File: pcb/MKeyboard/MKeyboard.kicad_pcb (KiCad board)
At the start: 6 copper layers, 57.1 x 114.3 mm, 90 parts, among them J1 USB_C_Receptacle_USB2.0, SW0 SW_Push, SW1 SW_Push, SW10 SW_Push, SW11 SW_Push, SW12 SW_Push, SW2 SW_Push, SW20 SW_Push, SW21 SW_Push, SW22 SW_Push, SW3 SW_DIP_x01, SW30 SW_Push, SW31 SW_Push, SW32 SW_Push, SW40 SW_Push, SW41 SW_Push, SW42 SW_Push, U1 AT90USB646-AU, Y1 Crystal_GND24

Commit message: placement
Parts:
- moved R33 41.6 mm to (106.6, 116.1), turned to 270 degrees
- moved R32 40.6 mm to (103.0, 116.1), turned to 270 degrees
- moved R31 40.0 mm to (99.6, 116.5), turned to 270 degrees
- moved C2 39.5 mm to (96.8, 96.0)
- moved C9 39.5 mm to (96.8, 108.7)
- moved R61 39.5 mm to (95.5, 115.1)
- moved C1 39.5 mm to (110.7, 92.2)
- moved C3 39.5 mm to (96.8, 102.4)
- moved C8 39.5 mm to (104.4, 92.2)
- moved R52 39.4 mm to (112.5, 151.0)
- moved R53 39.4 mm to (115.1, 151.0)
- moved R54 39.4 mm to (117.6, 151.0)
- moved U1 39.2 mm to (107.7, 103.5)
- moved R8 38.7 mm to (98.4, 149.1)
- moved R7 38.7 mm to (98.4, 151.6)
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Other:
- board size 57.1 x 114.3 mm -> 57.1 x 88.8 mm

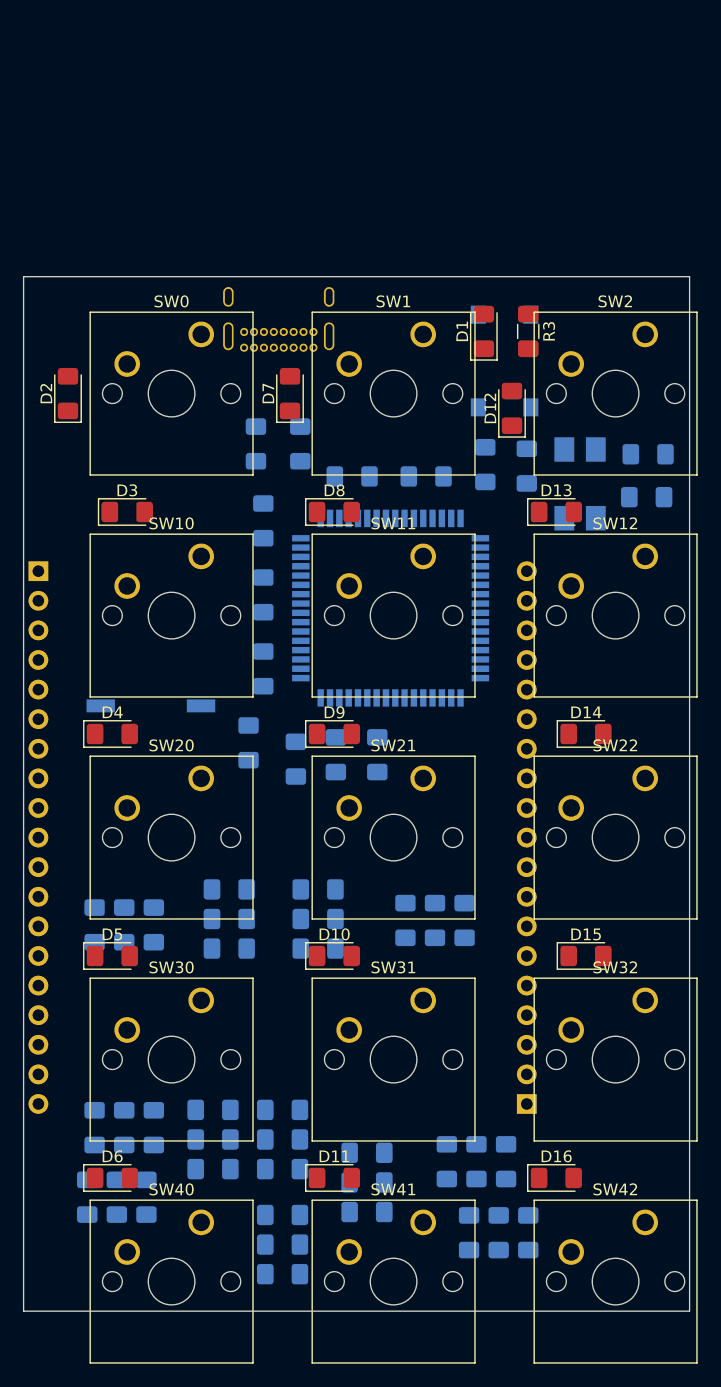
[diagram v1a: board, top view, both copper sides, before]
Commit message: smaller components, positioning
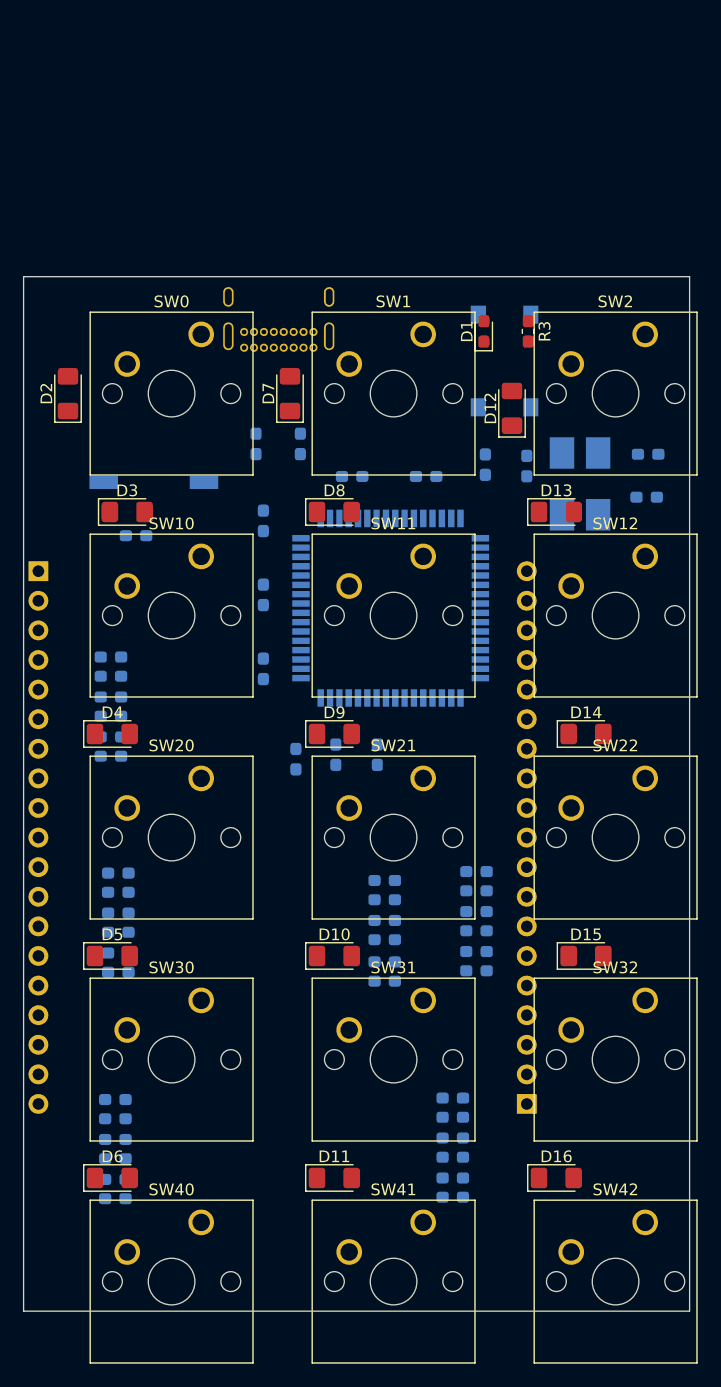
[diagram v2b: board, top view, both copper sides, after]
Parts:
- C1, C2, C3, C4, C5, C7, C8, C9: footprint Capacitor_SMD:C_1206_3216Metric_Pad1.42x1.75mm_HandSolder -> Capacitor_SMD:C_0603_1608Metric_Pad1.05x0.95mm_HandSolder
- D1: footprint LED_SMD:LED_1206_3216Metric_Pad1.42x1.75mm_HandSolder -> LED_SMD:LED_0603_1608Metric_Pad1.05x0.95mm_HandSolder
- R1, R10, R11, R12, R13, R14, R15, R16, R17, R18, R19, R2, R20, R21, R22, R23, R24, R25, R26, R27, R3, R31, R32, R33, R34, R35, R36, R4, R43, R44, R45, R5, R52, R53, R54, R58, R59, R6, R60, R61, R62, R7, R8, R9: footprint Resistor_SMD:R_1206_3216Metric_Pad1.42x1.75mm_HandSolder -> Resistor_SMD:R_0603_1608Metric_Pad1.05x0.95mm_HandSolder
- Y1: footprint Crystal:Crystal_SMD_7050-4Pin_7.0x5.0mm -> Crystal:Crystal_SMD_0603-4Pin_6.0x3.5mm_HandSoldering
- moved R54 26.3 mm to (107.2, 126.9), turned to 0 degrees
- moved R27 23.0 mm to (83.7, 107.7), turned to 0 degrees
- moved R53 22.1 mm to (107.2, 130.3), turned to 0 degrees
- moved R21 21.9 mm to (84.3, 126.2), turned to 0 degrees
- moved R24 20.9 mm to (83.7, 109.3)
- moved R15 20.4 mm to (84.3, 127.9)
- moved R61 20.2 mm to (85.9, 97.3), turned to 180 degrees
- moved R23 20.1 mm to (83.7, 112.8)
- moved R9 20.1 mm to (107.2, 128.5)
- moved R26 19.6 mm to (83.7, 111.1), turned to 0 degrees
- moved R14 19.5 mm to (84.3, 131.3)
- moved R22 19.4 mm to (83.7, 116.2)
- moved R8 19.3 mm to (107.2, 132.0)
- moved SW3 19.2 mm to (87.4, 92.7)
- moved R13 18.7 mm to (84.3, 134.7)
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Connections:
- J1 pad A5: Net-(J1-PadA5) -> (no net)
- J1 pad A8: Net-(J1-PadA8) -> (no net)
- J1 pad B5: Net-(J1-PadB5) -> (no net)
- J1 pad B8: Net-(J1-PadB8) -> (no net)
- U1 pad 1: Net-(U1-Pad1) -> (no net)
- U1 pad 10: Net-(U1-Pad10) -> (no net)
- U1 pad 11: Net-(U1-Pad11) -> (no net)
- U1 pad 12: Net-(U1-Pad12) -> (no net)
- U1 pad 13: Net-(U1-Pad13) -> (no net)
- U1 pad 14: Net-(U1-Pad14) -> (no net)
- U1 pad 15: Net-(U1-Pad15) -> (no net)
- U1 pad 16: Net-(U1-Pad16) -> (no net)
- U1 pad 17: Net-(U1-Pad17) -> (no net)
- U1 pad 18: Net-(U1-Pad18) -> (no net)
- U1 pad 19: Net-(U1-Pad19) -> (no net)
- U1 pad 2: Net-(U1-Pad2) -> (no net)
- U1 pad 54: Net-(U1-Pad54) -> (no net)
- U1 pad 55: Net-(U1-Pad55) -> (no net)
- U1 pad 56: Net-(U1-Pad56) -> (no net)
- U1 pad 57: Net-(U1-Pad57) -> (no net)
- U1 pad 58: Net-(U1-Pad58) -> (no net)
- U1 pad 59: Net-(U1-Pad59) -> (no net)
- U1 pad 60: Net-(U1-Pad60) -> (no net)
- U1 pad 61: Net-(U1-Pad61) -> (no net)
- U1 pad 62: Net-(U1-Pad62) -> (no net)
- U1 pad 9: Net-(U1-Pad9) -> (no net)

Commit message: Most 0-ohm resisters are routed.
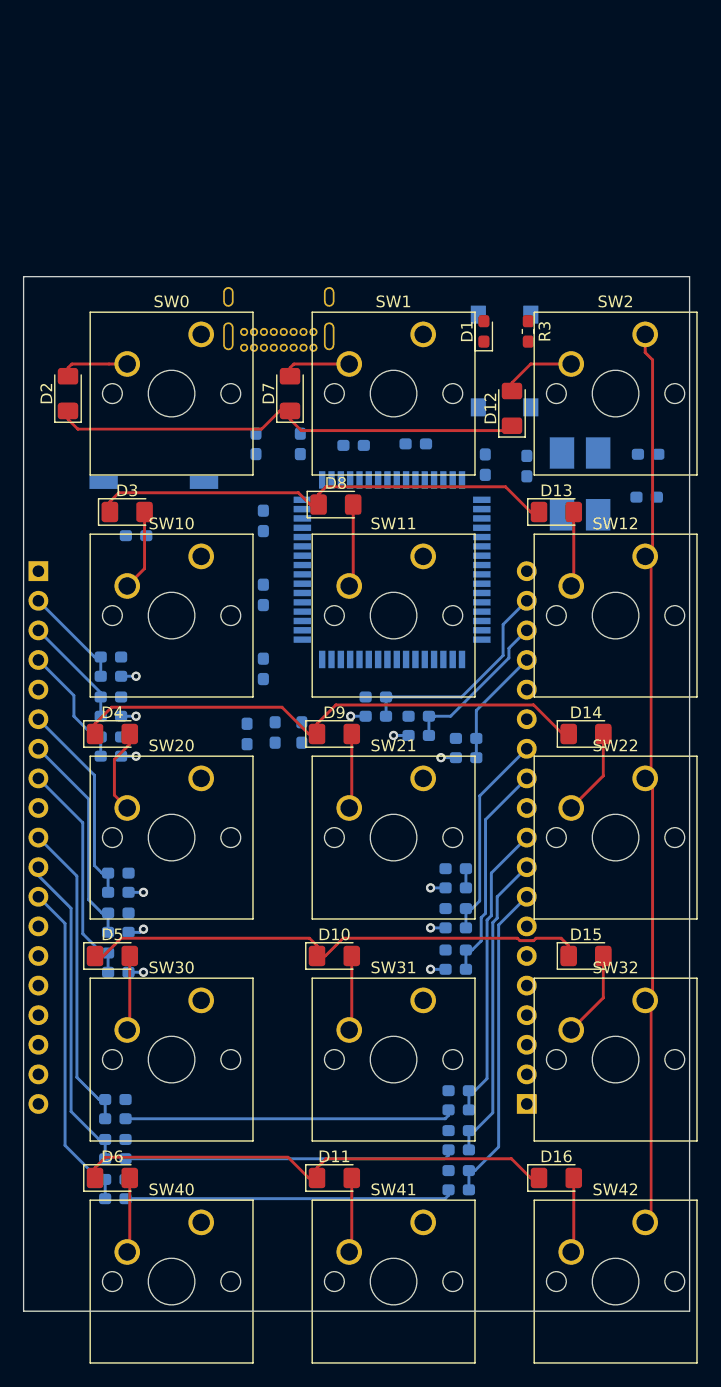
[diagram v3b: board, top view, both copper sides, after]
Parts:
- moved R16 18.3 mm to (114.2, 116.3)
- moved R58 18.3 mm to (114.2, 114.7)
- moved R17 17.5 mm to (110.1, 114.4)
- moved R59 17.5 mm to (110.1, 112.8)
- moved R18 17.3 mm to (106.4, 112.8)
- moved R60 17.3 mm to (106.4, 111.1)
- moved R33 6.75 mm to (100.1, 114.2)
- moved R54 6.18 mm to (113.3, 125.9)
- moved R9 6.18 mm to (113.3, 127.5)
- moved R52 6.18 mm to (113.3, 132.8)
- moved R53 6.18 mm to (113.3, 129.3)
- moved R7 6.18 mm to (113.3, 134.5)
- moved R8 6.18 mm to (113.3, 130.9)
- moved R32 5.54 mm to (97.8, 114.2)
- moved R31 4.71 mm to (95.4, 114.3)
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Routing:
- net /col2: track 0.00 -> 106.4 mm
- net /col1: track 0.00 -> 105.9 mm
- net /col0: track 0.00 -> 105.5 mm
- net /con_l0_0: track 0.00 -> 67.0 mm, vias 0 -> 1
- net /con_l0_1: track 0.00 -> 65.8 mm, vias 0 -> 1
- net /con_l0_2: track 0.00 -> 64.5 mm, vias 0 -> 1
- net /con_r0_0: track 0.00 -> 64.4 mm, vias 0 -> 1
- net /con_r0_1: track 0.00 -> 63.1 mm, vias 0 -> 1
- net /con_r0_2: track 0.00 -> 61.9 mm, vias 0 -> 1
- net /con_r1_0: track 0.00 -> 58.1 mm, vias 0 -> 1
- net /con_l1_0: track 0.00 -> 56.0 mm, vias 0 -> 1
- net /con_r1_1: track 0.00 -> 55.1 mm, vias 0 -> 1
- net /con_l1_1: track 0.00 -> 52.4 mm, vias 0 -> 1
- net /con_l1_2: track 0.00 -> 49.1 mm, vias 0 -> 1
- net /row2: track 0.00 -> 45.6 mm
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
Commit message: Most of the non-power routing.
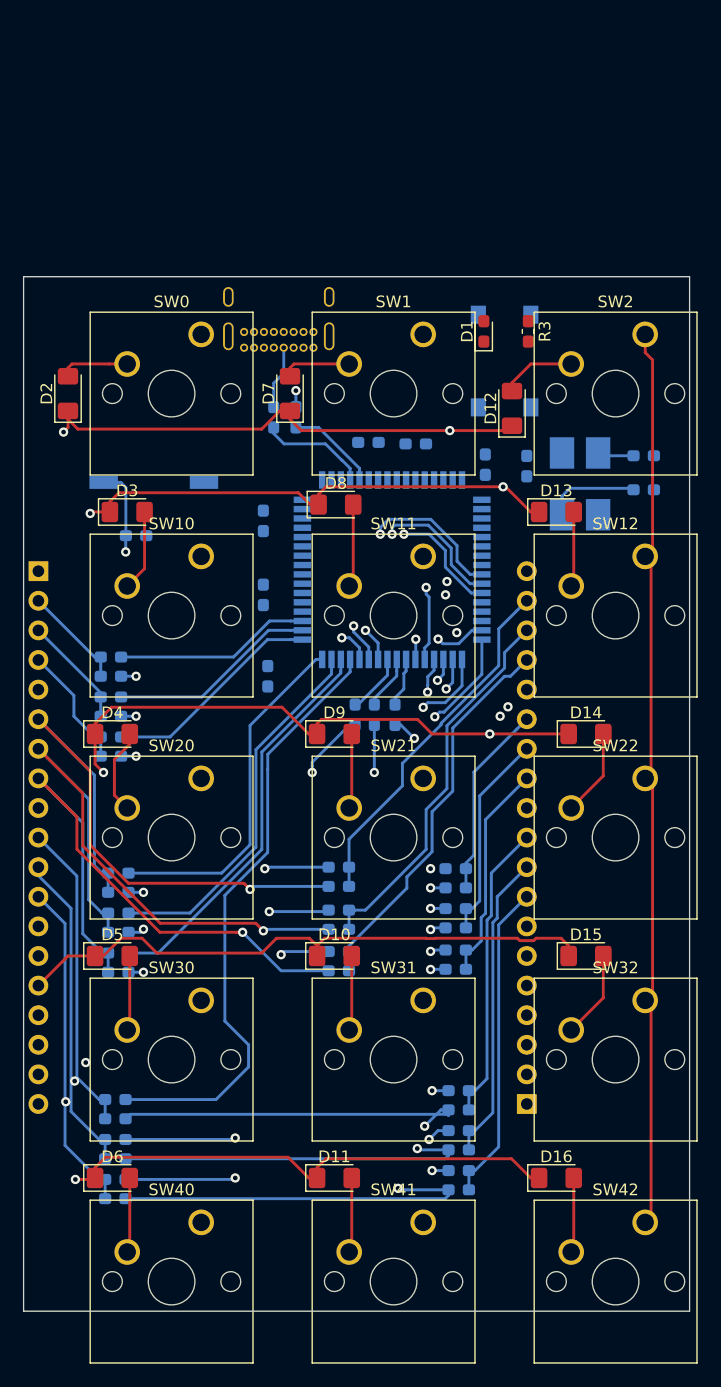
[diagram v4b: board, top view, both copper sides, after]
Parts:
- moved R16 21.3 mm to (103.3, 134.6)
- moved R58 21.3 mm to (103.3, 133.0)
- moved R59 18.0 mm to (103.3, 129.4)
- moved R17 18.0 mm to (103.3, 131.1)
- moved R18 14.9 mm to (103.3, 127.4)
- moved R60 14.9 mm to (103.3, 125.7)
- moved R31 9.42 mm to (104.6, 112.6), turned to 90 degrees
- moved R32 8.64 mm to (106.3, 112.6), turned to 90 degrees
- moved R33 8.14 mm to (108.1, 112.6), turned to 90 degrees
- moved R1 4.12 mm to (99.6, 87.1)
- moved C4 3.57 mm to (129.4, 90.4)
- moved R2 3.23 mm to (97.7, 87.1), turned to 90 degrees
- moved C7 3.07 mm to (129.4, 93.3)
- moved C8 1.30 mm to (105.8, 89.3)
- moved C9 0.74 mm to (97.2, 109.3)
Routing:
- net /row0: track 41.1 -> 168.0 mm, vias 0 -> 4
- net /row1: track 40.5 -> 155.8 mm, vias 0 -> 4
- net /row4: track 42.0 -> 142.8 mm, vias 0 -> 3
- net /row2: track 45.6 -> 132.1 mm, vias 0 -> 4
- net /row3: track 44.4 -> 130.6 mm, vias 0 -> 2
- net /cp8: track 0.00 -> 64.0 mm, vias 0 -> 2
- net /cp14: track 0.00 -> 63.7 mm, vias 0 -> 2
- net /cp13: track 0.00 -> 61.1 mm, vias 0 -> 2
- net /cp12: track 0.00 -> 60.4 mm, vias 0 -> 2
- net /cp7: track 0.00 -> 59.1 mm, vias 0 -> 2
- net /cp18: track 0.00 -> 56.4 mm, vias 0 -> 2
- net /cp19: track 0.00 -> 55.2 mm, vias 0 -> 2
- net /cp20: track 0.00 -> 52.1 mm, vias 0 -> 2
- net /cp6: track 0.00 -> 52.0 mm
- net /col2: track 106.4 -> 155.7 mm, vias 0 -> 2
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
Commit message: power planes and all components routed
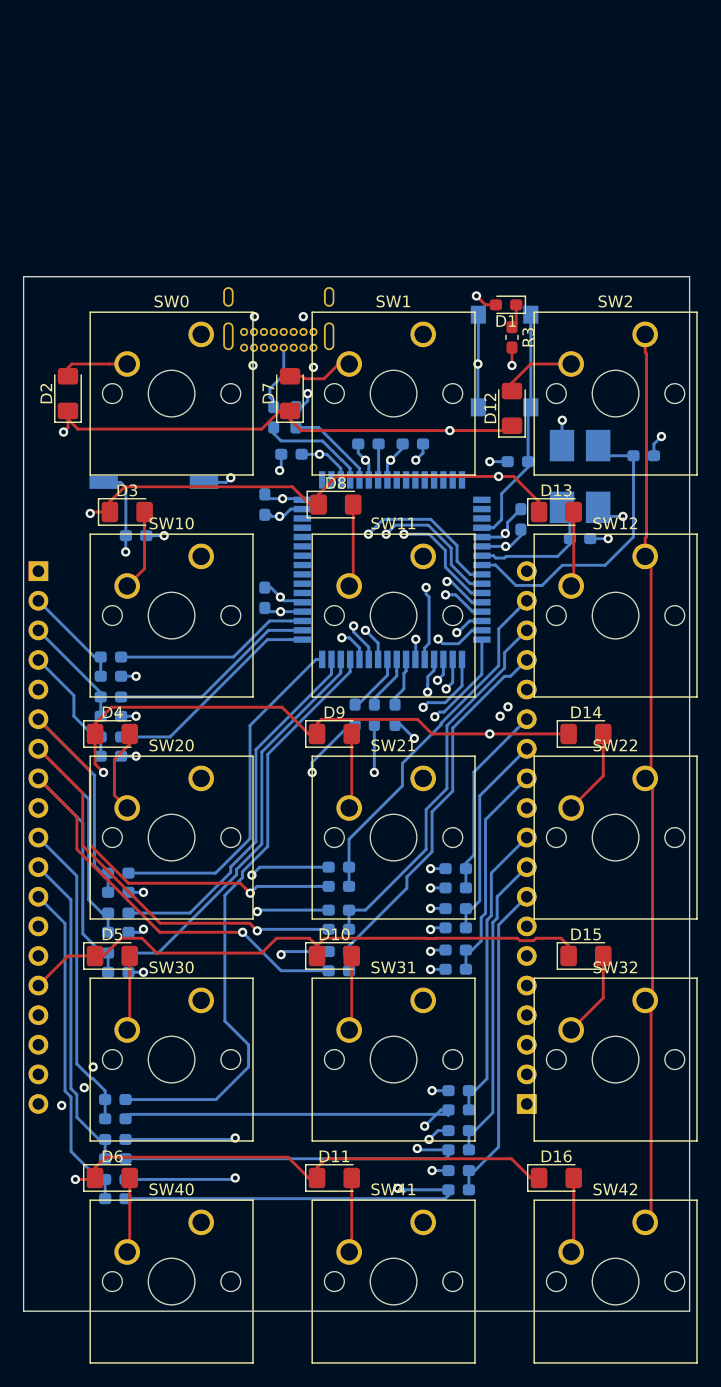
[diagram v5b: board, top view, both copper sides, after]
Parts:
- moved C9 19.2 mm to (99.2, 90.3), turned to 180 degrees
- moved C7 6.88 mm to (124.0, 97.5)
- moved C5 5.60 mm to (118.9, 95.9)
- moved D1 2.98 mm to (117.6, 77.5), turned to 180 degrees
- moved R3 1.49 mm to (118.1, 80.3)
- moved C2 1.40 mm to (96.9, 94.6), turned to 270 degrees
- moved R62 0.85 mm to (118.6, 90.9), turned to 0 degrees
- moved Y1 0.64 mm to (124.0, 92.2)
- moved C3 0.28 mm to (96.9, 102.6), turned to 90 degrees
- moved C1 0.25 mm to (109.6, 89.4)
- moved C8 0.13 mm to (105.8, 89.4)
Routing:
- net VCC: track 2.70 -> 34.3 mm, vias 0 -> 12
- net GND: track 13.7 -> 44.3 mm, vias 0 -> 13
- net Net-(C4-Pad1): track 3.13 -> 25.6 mm
- net Net-(R62-Pad2): track 0.00 -> 21.5 mm
- net /cp17: track 28.7 -> 33.7 mm
- net /cp20: track 52.1 -> 56.3 mm
- net /cp16: track 31.9 -> 35.6 mm
- net Net-(C7-Pad1): track 8.07 -> 11.6 mm
- net /cp18: track 56.4 -> 59.6 mm
- net Net-(C8-Pad1): track 0.00 -> 3.11 mm
- net /row1: track 155.8 -> 158.8 mm
- net /cp19: track 55.2 -> 58.1 mm
- net /cp15: track 32.8 -> 35.4 mm
- net Net-(D1-Pad1): track 0.00 -> 2.07 mm
- net Net-(J1-PadA6): track 7.58 -> 8.70 mm
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- added copper zone on In4.Cu, net GND
- added copper zone on In1.Cu, net VCC
